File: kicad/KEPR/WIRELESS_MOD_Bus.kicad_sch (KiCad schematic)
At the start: 1 part, among them J4 Conn_02x08_Odd_Even

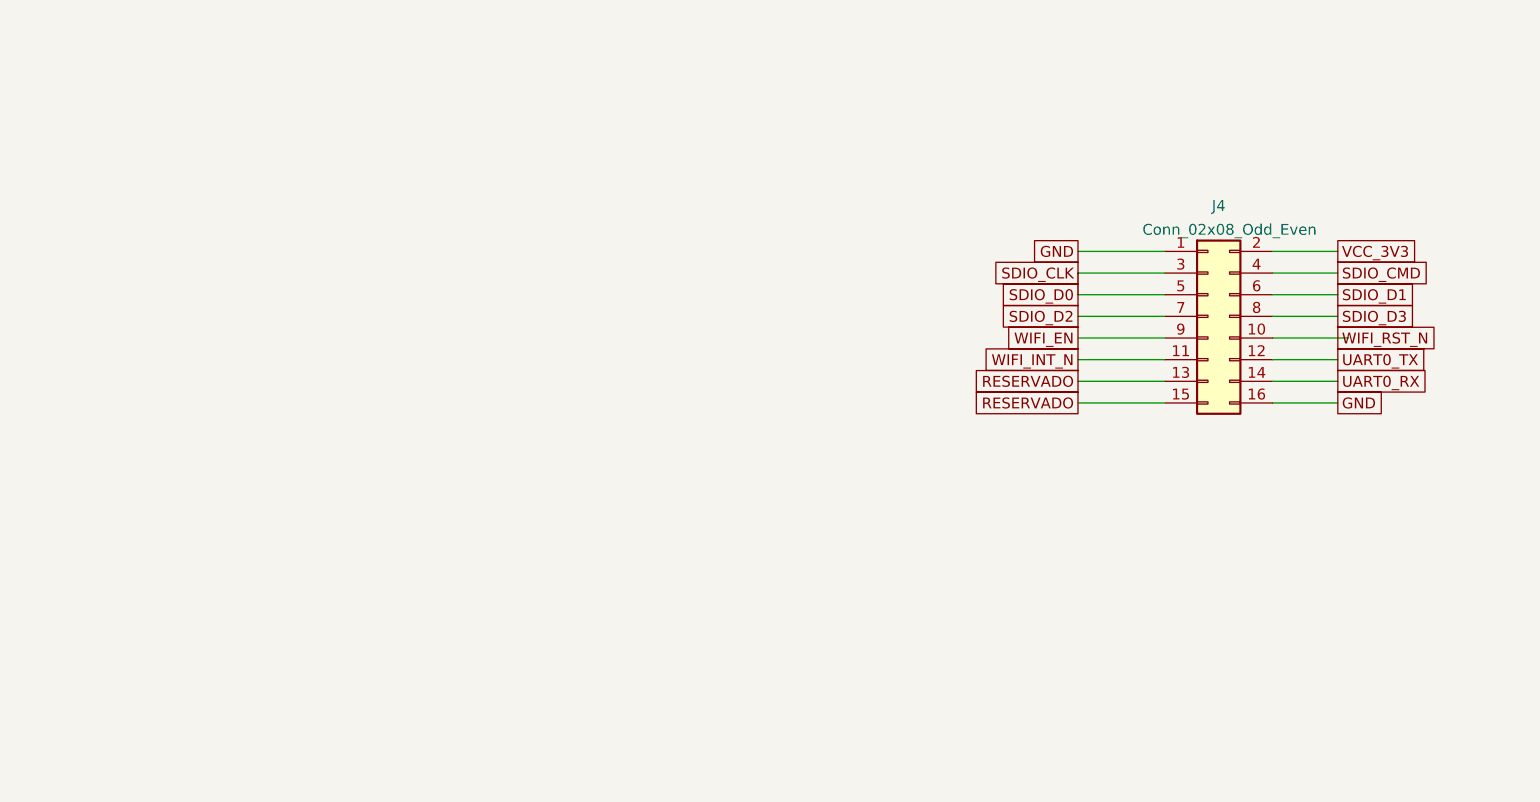
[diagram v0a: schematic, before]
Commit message: Adicinado o barramento externo
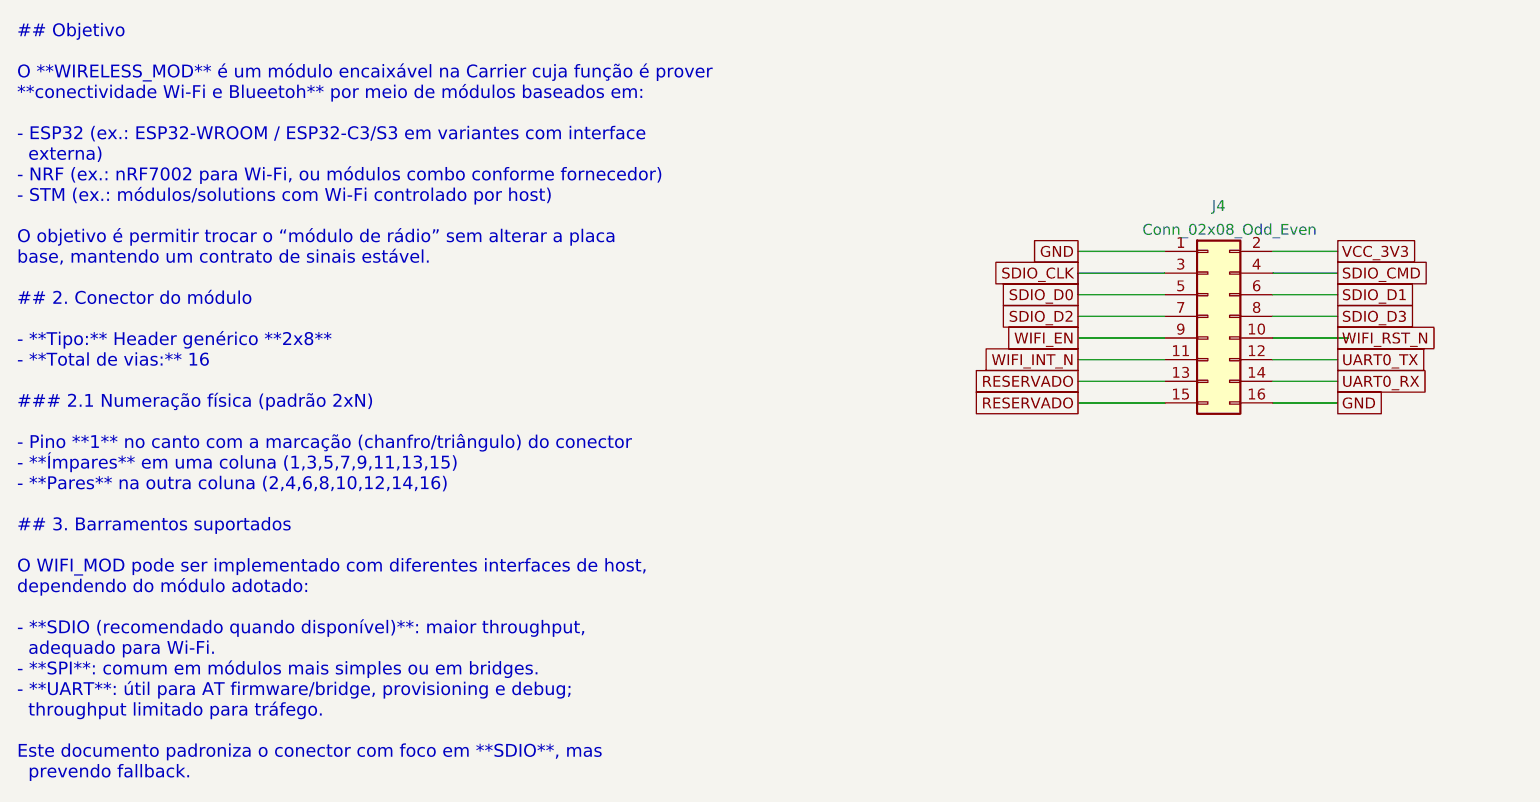
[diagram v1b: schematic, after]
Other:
- note added: "## Objetivo O **WIRELESS_MOD** é um módulo encaixável na Carrier cuja função é prover **conectividade Wi‑Fi e Blueetoh** por meio de módulos baseados em: - ESP32 (ex.: ESP32-WROOM / ESP32-C3/S3 em variantes com interface externa) - NRF (ex.: nRF7002 para Wi‑Fi, ou módulos combo conforme fornecedor) - STM (ex.: módulos/solutions com Wi‑Fi controlado por host) O objetivo é permitir trocar o “módulo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"

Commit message: Iniciado projeto da PCB, para uma referência de tamanho.
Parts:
- J5: renamed from J4; footprint (none) -> Connector_IDC:IDC-Header_2x08_P2.54mm_Latch12.0mm_Vertical
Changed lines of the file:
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@@
 		(on_board yes)
 		(dnp no)
-		(property "Reference" "J?"
+		(property "Reference" "J5"
 			(at 207.01 119.126 0)
 			(effects
@@
 			)
 		)
-		(property "Footprint" ""
-			(at 205.74 132.08 0)
+		(property "Footprint" "Connector_IDC:IDC-Header_2x08_P2.54mm_Latch12.0mm_Vertical"
+			(at 205.74 116.84 0)
 			(effects
 				(font
 					(size 1.27 1.27)
 				)
-				(hide yes)
 			)
 		)
@@
 			(project "KEPR"
 				(path "/5d9e1dfb-5ec5-4e06-bbdb-9cbfa1c0b9f1/0260e008-78ae-4c2c-85f8-b31739d2ea08/89baefaa-37bd-4fe5-ae03-63909fd895b0"
-					(reference "J?")
+					(reference "J5")
 					(unit 1)
 				)

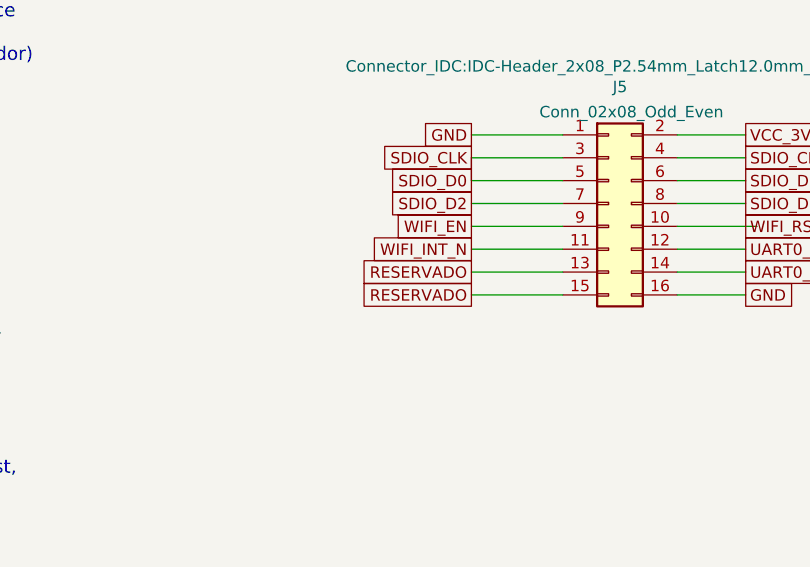
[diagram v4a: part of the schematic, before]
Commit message: Iniciado a distribuição das vias.
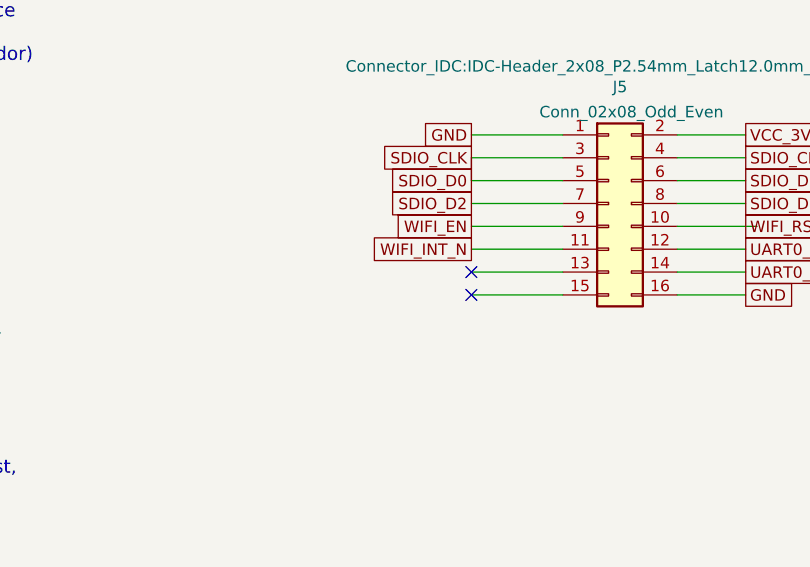
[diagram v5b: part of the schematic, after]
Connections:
- net RESERVADO: no longer names the net of J5.13 (Pin_13)
- net RESERVADO: no longer J5.15 (Pin_15)
- no-connect marks 0 -> 2
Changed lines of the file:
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@@
 		)
+	)
+	(no_connect
+		(at 190.5 139.7)
+	)
+	(no_connect
+		(at 190.5 142.24)
 	)
 	(wire
@@
 		)
 	)
-	(global_label "RESERVADO"
-		(shape passive)
-		(at 190.5 139.7 180)
-		(effects
-			(font
-				(size 1.27 1.27)
-			)
-			(justify right bottom)
-		)
-		(property "Intersheetrefs" "${INTERSHEET_REFS}"
-			(at 190.5 139.7 0)
-			(effects
-				(font
-					(size 1.27 1.27)
-				)
-				(justify right)
-				(hide yes)
-			)
-		)
-	)
 	(global_label "SDIO_D2"
 		(shape passive)
@@
 			(effects
 				(font
-					(size 1.27 1.27)
-				)
-				(justify right)
-				(hide yes)
-			)
-		)
-	)
-	(global_label "RESERVADO"
-		(shape passive)
-		(at 190.5 142.24 180)
-		(effects
-			(font
-				(size 1.27 1.27)
-			)
-			(justify right bottom)
-		)
-		(property "Intersheetrefs" "${INTERSHEET_REFS}"
-			(at 190.5 142.24 0)
-			(effects
-				(font
